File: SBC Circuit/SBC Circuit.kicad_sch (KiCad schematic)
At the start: 27 parts, among them J3 Conn_01x06_Pin, SW1 RESET, U1 MC68000FN, U11 MC34064P, U2 XC9572XL, X1 SG-531

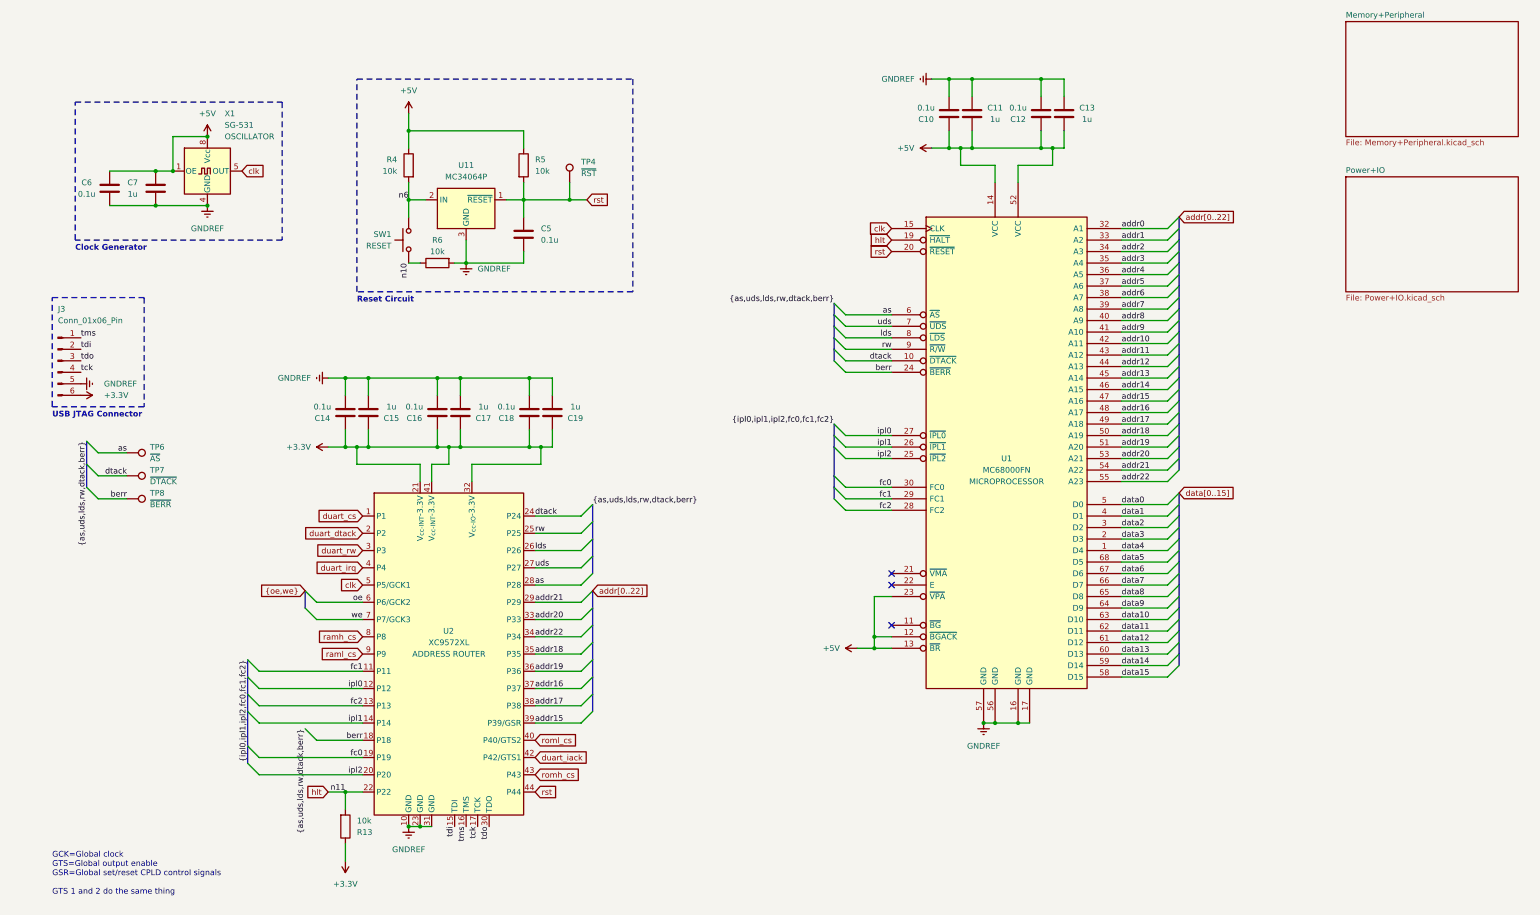
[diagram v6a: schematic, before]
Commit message: Finalize PCB, neaten up Schematic
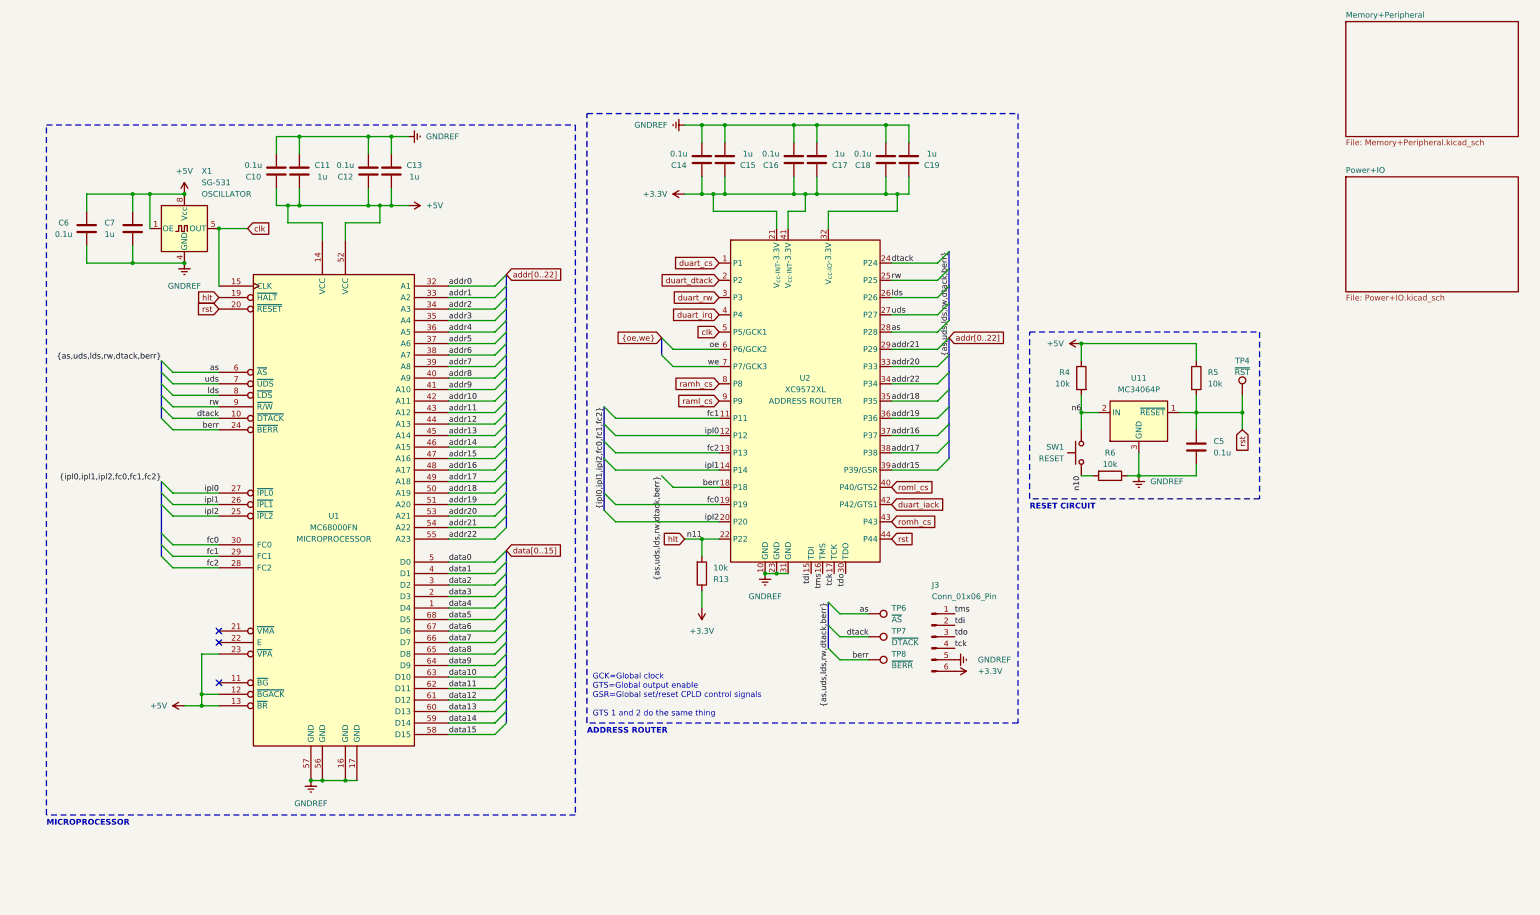
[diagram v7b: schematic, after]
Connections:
- net GNDREF: now also R6.1; no longer R6.2
- net n10: now also R6.2; no longer R6.1
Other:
- note added: "ADDRESS ROUTER"
- note added: "MICROPROCESSOR"
- note added: "RESET CIRCUIT"
- note removed: "Clock Generator"
- note removed: "Reset Circuit"
- note removed: "USB JTAG Connector"
- moved on the sheet: C10, C11, C12, C13, C14, C15, C16, C17, C18, C19, C5, C6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
